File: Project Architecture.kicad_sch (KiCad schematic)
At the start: 0 parts

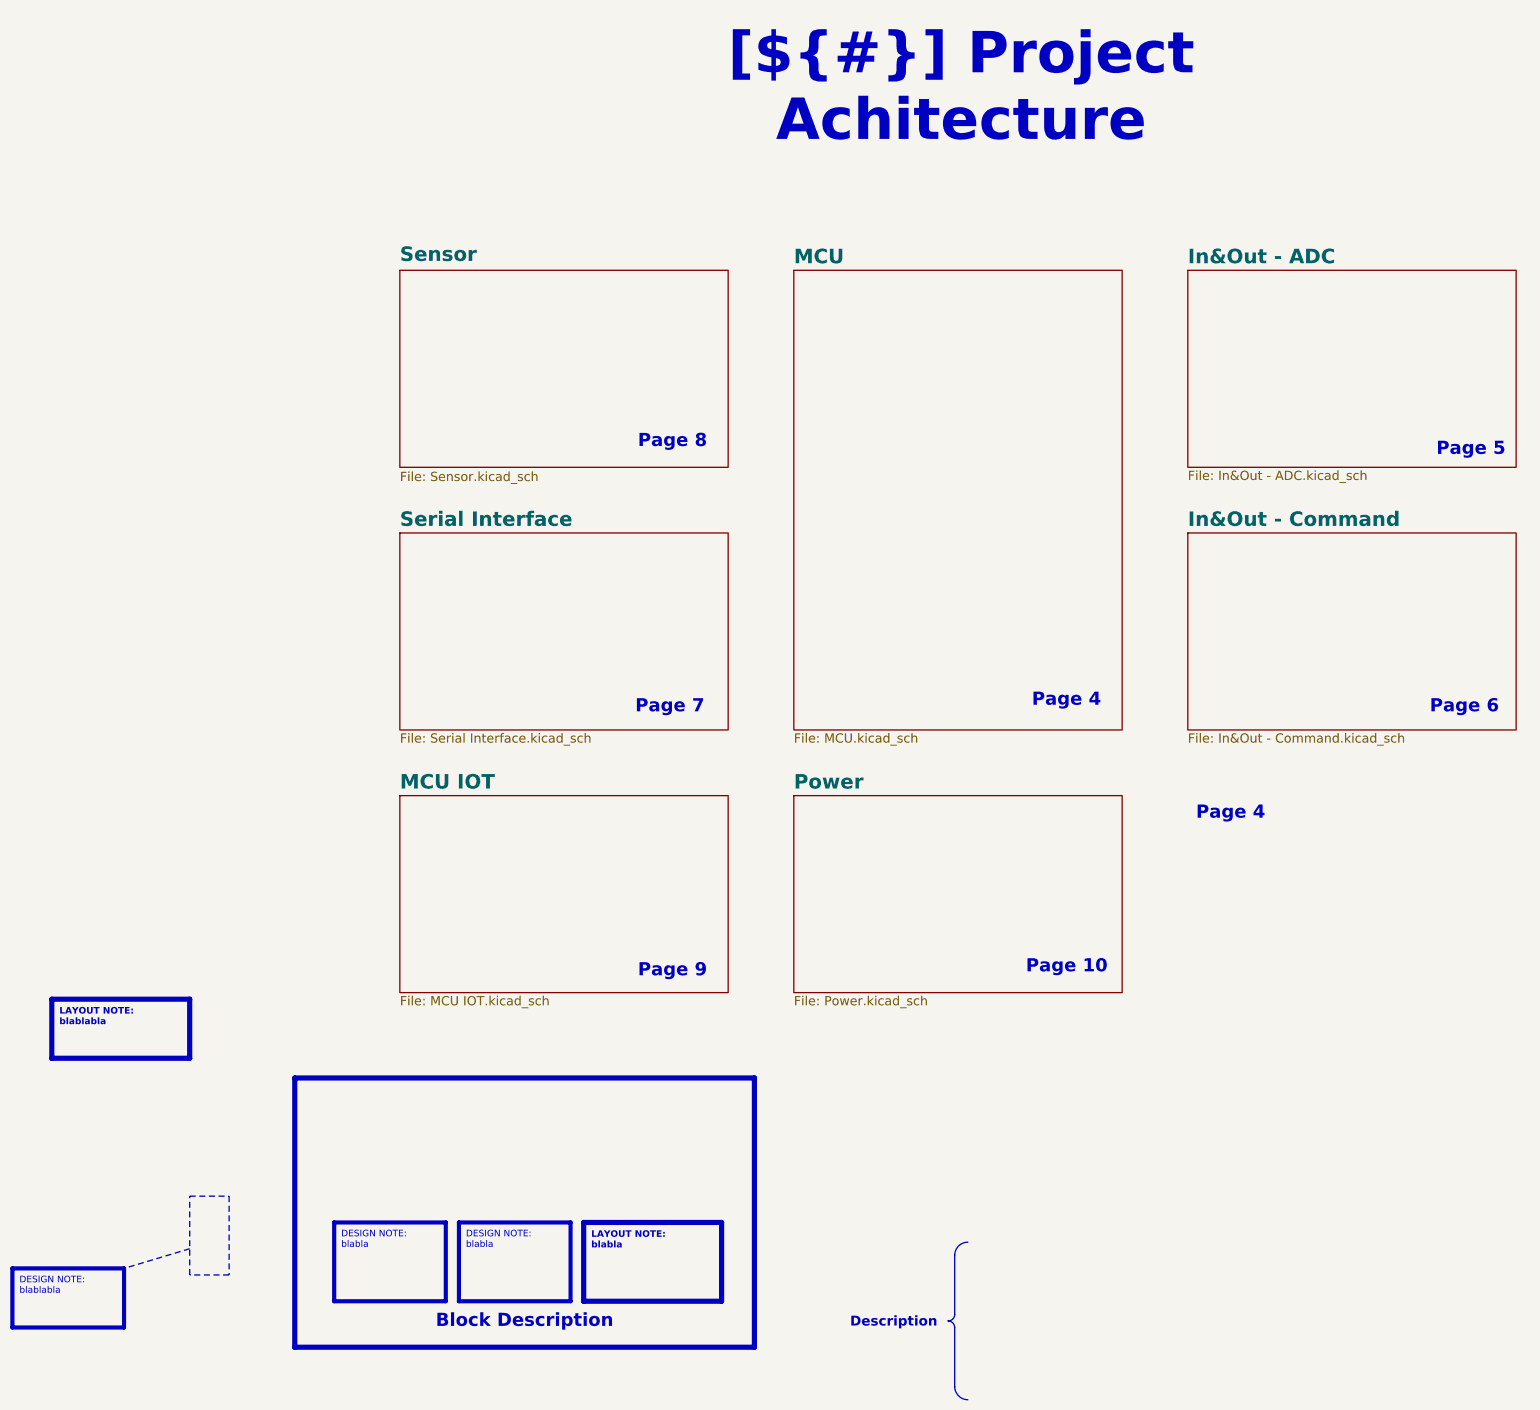
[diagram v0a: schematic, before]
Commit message: [Project][Added] CI/CD environment
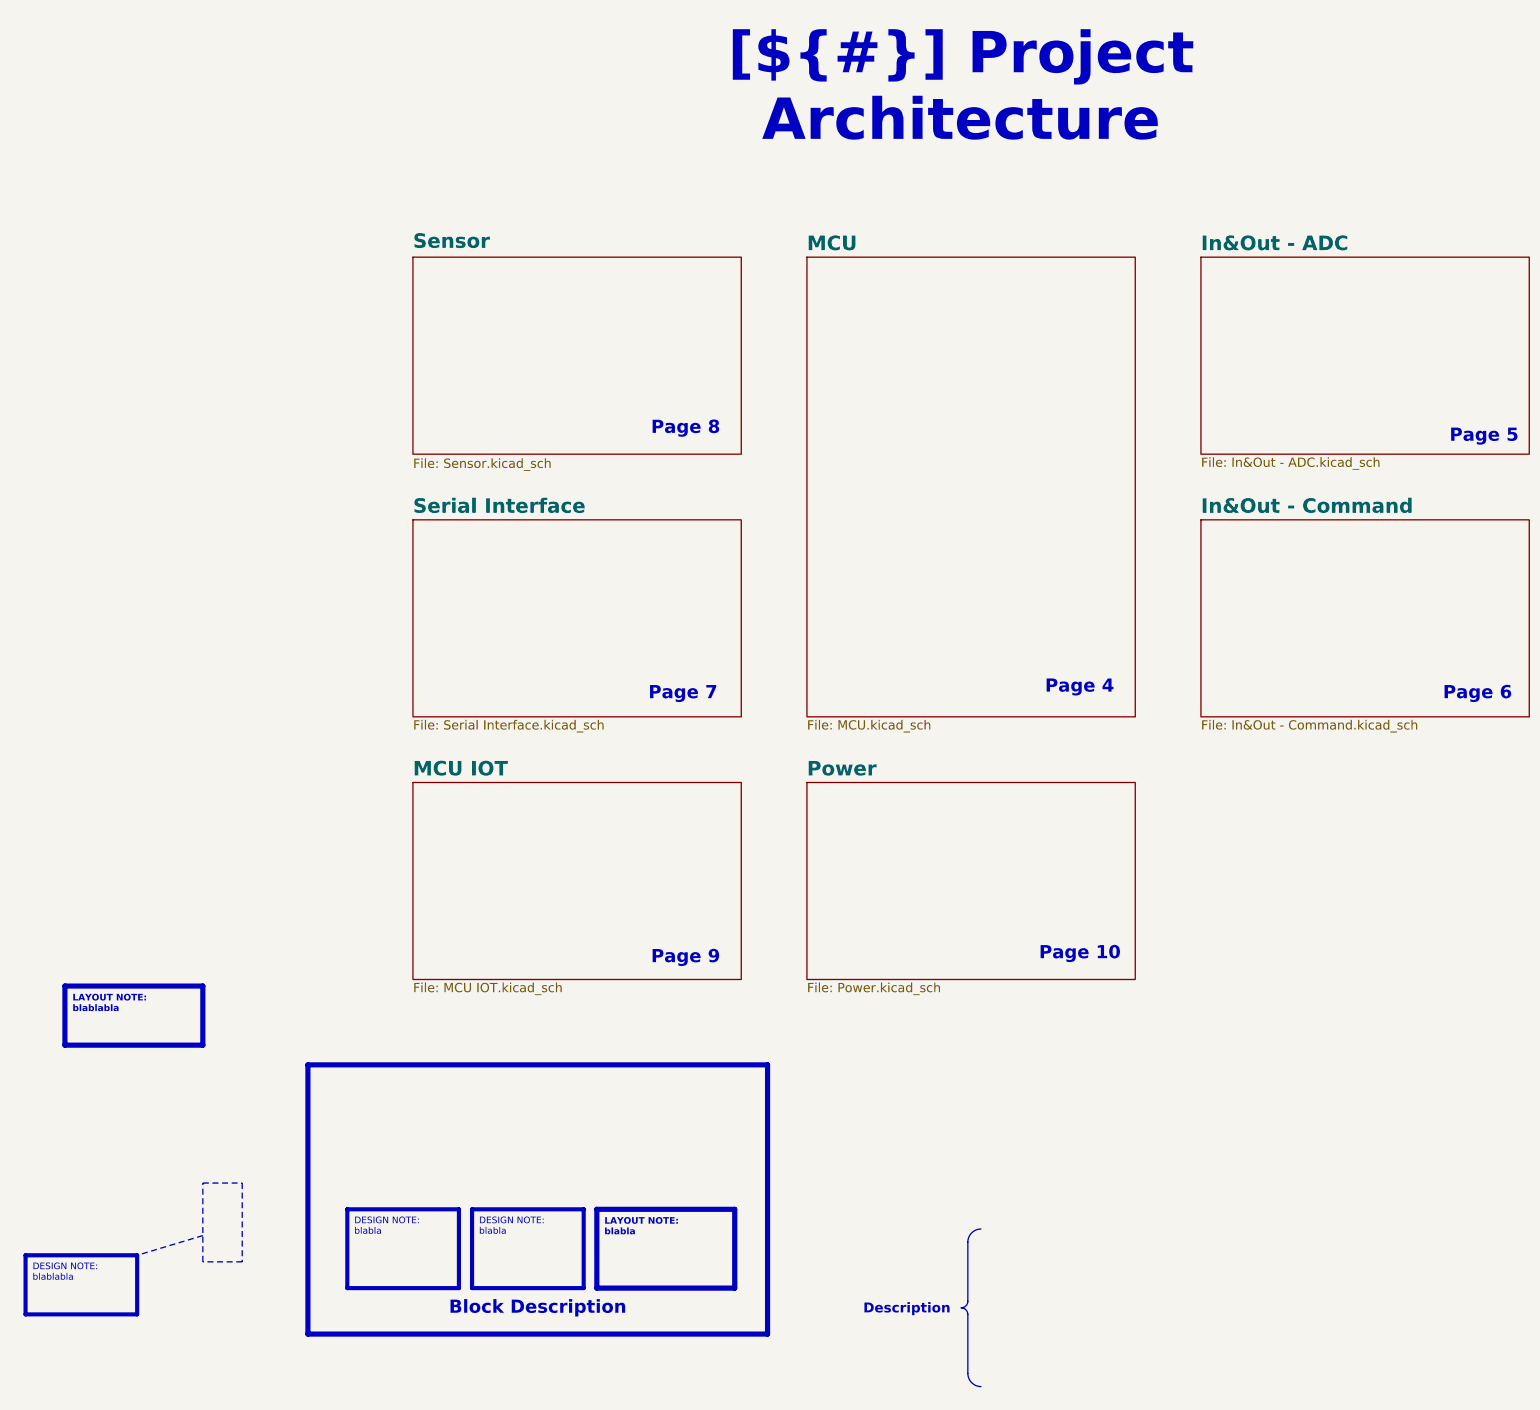
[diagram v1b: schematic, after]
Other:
- title: Project Achitecture -> Project Architecture

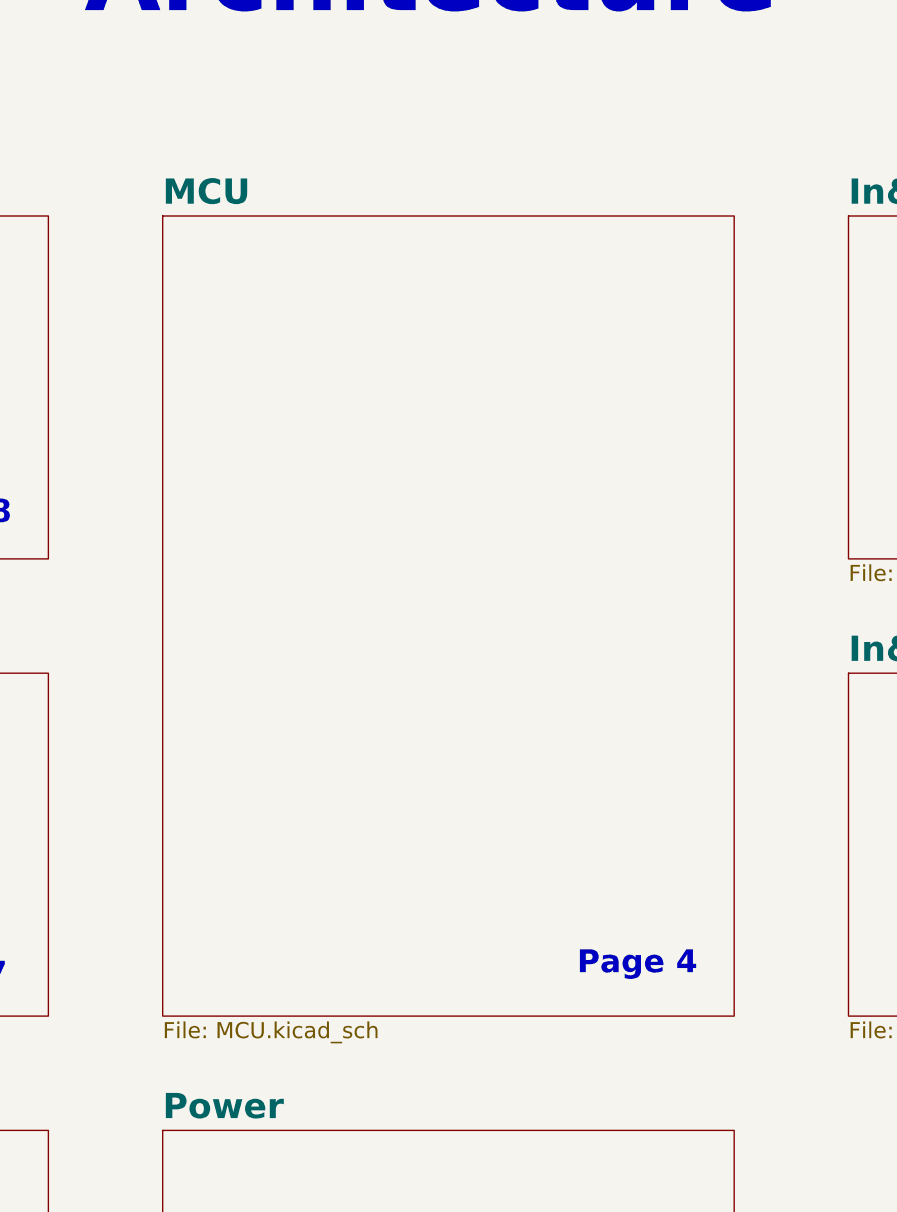
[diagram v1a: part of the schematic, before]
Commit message: [Schematic][Add] Add of a new page : MCU Expander
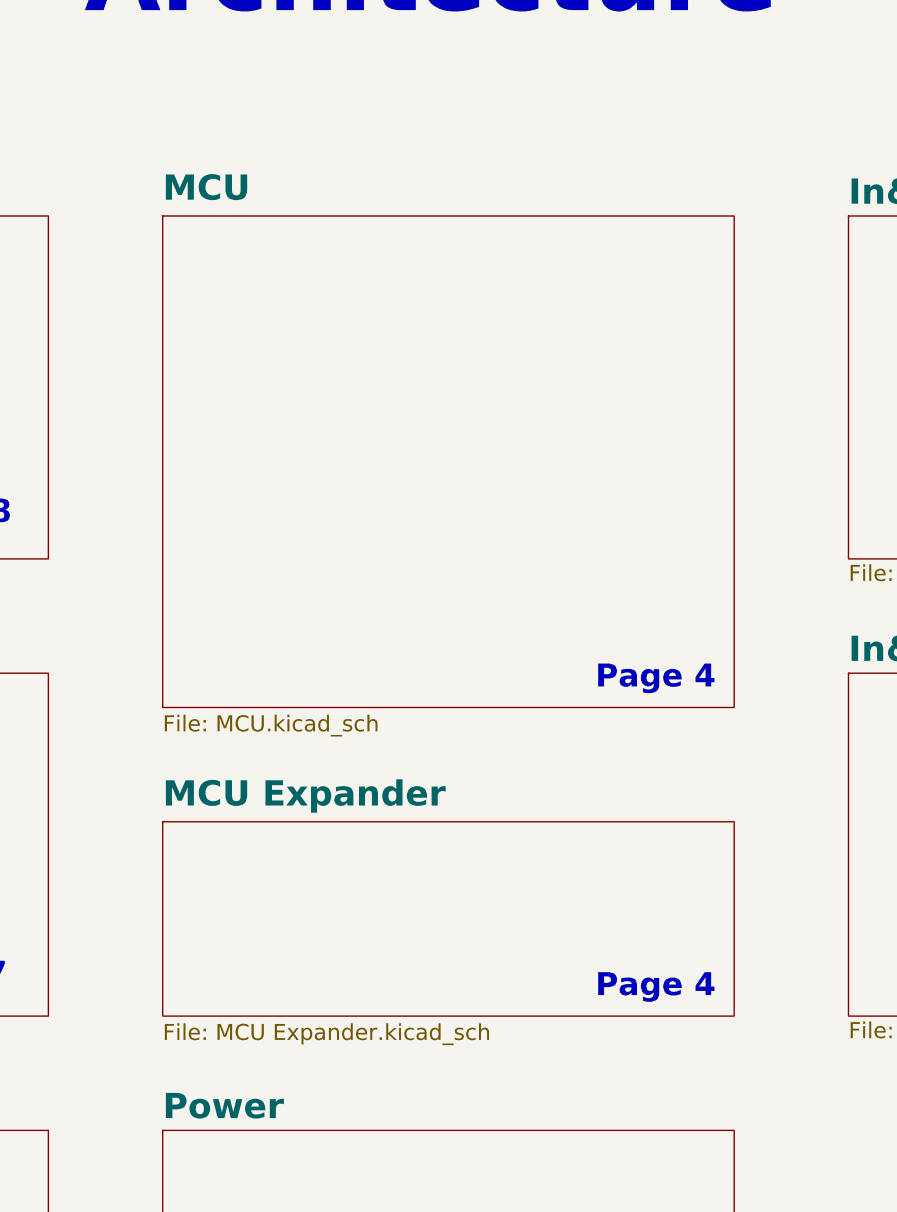
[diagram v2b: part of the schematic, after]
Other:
- added sheet MCU Expander (MCU Expander.kicad_sch)
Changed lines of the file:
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@@
 	(text "Page 4"
 		(exclude_from_sim no)
-		(at 239.776 145.542 0)
+		(at 241.808 113.792 0)
 		(effects
 			(font
@@
 			(justify right bottom)
 			(href "#5")
+		)
+	)
+	(text "Page 4"
+		(exclude_from_sim no)
+		(at 241.808 148.082 0)
+		(effects
+			(font
+				(size 2.54 2.54)
+				(bold yes)
+				(color 0 0 255 0.7490196078)
+			)
+			(justify right bottom)
+			(href "#4")
 		)
 	)
@@
 			(project "Data-Acquisition-Board"
 				(path "/f9e05184-c88b-4a88-ae9c-ab2bdb32be7c/c5103ceb-5325-4a84-a025-9638a412984e"
-					(page "10")
+					(page "11")
 				)
 			)
@@
 			(project "Data-Acquisition-Board"
 				(path "/f9e05184-c88b-4a88-ae9c-ab2bdb32be7c/c5103ceb-5325-4a84-a025-9638a412984e"
-					(page "6")
+					(page "8")
 				)
 			)
@@
 			(project "Data-Acquisition-Board"
 				(path "/f9e05184-c88b-4a88-ae9c-ab2bdb32be7c/c5103ceb-5325-4a84-a025-9638a412984e"
-					(page "5")
+					(page "7")
 				)
 			)
@@
 			(project "Data-Acquisition-Board"
 				(path "/f9e05184-c88b-4a88-ae9c-ab2bdb32be7c/c5103ceb-5325-4a84-a025-9638a412984e"
-					(page "7")
+					(page "9")
+				)
+			)
+		)
+	)
+	(sheet
+		(at 180.34 128.27)
+		(size 63.5 21.59)
+		(exclude_from_sim no)
+		(in_bom yes)
+		(on_board yes)
+		(dnp no)
+		(fields_autoplaced yes)
+		(stroke
+			(width 0.1524)
+			(type solid)
+		)
+		(fill
+			(color 1 101 252 0.6510)
+		)
+		(property "Sheetname" "MCU Expander"
+			(at 180.34 126.7964 0)
+			(effects
+				(font
+					(face "Times New Roman")
+					(size 2.794 2.794)
+					(bold yes)
+					(color 0 0 194 0.9019607843)
+				)
+				(justify left bottom)
+			)
+		)
+		(property "Sheetfile" "MCU Expander.kicad_sch"
+			(at 180.34 150.6478 0)
+			(effects
+				(font
+					(face "Arial")
+					(size 1.778 1.778)
+				)
+				(justify left top)
+			)
+		)
+		(instances
+			(project "Data-Acquisition-Board"
+				(path "/f9e05184-c88b-4a88-ae9c-ab2bdb32be7c/c5103ceb-5325-4a84-a025-9638a412984e"
+					(page "5")
 				)
 			)
@@
 			(project "Data-Acquisition-Board"
 				(path "/f9e05184-c88b-4a88-ae9c-ab2bdb32be7c/c5103ceb-5325-4a84-a025-9638a412984e"
-					(page "8")
+					(page "10")
 				)
 			)
@@
 	(sheet
 		(at 180.34 60.96)
-		(size 63.5 88.9)
+		(size 63.5 54.61)
 		(exclude_from_sim no)
 		(in_bom yes)
@@
 		)
 		(property "Sheetname" "MCU"
-			(at 180.34 59.9309 0)
+			(at 180.34 59.4864 0)
 			(effects
 				(font
@@
 		)
 		(property "Sheetfile" "MCU.kicad_sch"
-			(at 180.34 150.4446 0)
+			(at 180.34 116.3578 0)
 			(effects
 				(font
@@
 			(project "Data-Acquisition-Board"
 				(path "/f9e05184-c88b-4a88-ae9c-ab2bdb32be7c/c5103ceb-5325-4a84-a025-9638a412984e"
-					(page "9")
-				)
-			)
+					(page "6")
+				)
+			)

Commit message: [Schematic][Modify] Block Diagram
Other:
- sheet In&Out - ADC ports: added {MCU_ADC}; removed none
- sheet In&Out - Command ports: added {MCU_PWM}; removed none
- sheet MCU ports: added {MCU_ADC}, {MCU_PWM}, {MCU_Serial_COM}; removed none
- sheet MCU Expander ports: added {MCU_Serial_COM}; removed none
- sheet MCU IOT ports: added {ESP_Serial_COM}, {MCU_Serial_COM}; removed none
- sheet Sensor ports: added {ESP_Serial_COM}, {MCU_Serial_COM}; removed none
- sheet Serial Interface ports: added {MCU_Serial_COM}; removed none
- note added: "Page 11"
